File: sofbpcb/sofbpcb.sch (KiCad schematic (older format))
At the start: 18 parts, among them J1 MAX98357A_hdr, J2 MPU6050_hdr, J3 Conn_01x02_Male, J4 LEDStalk_hdr, J5 VibrationMotor_hdr, U1 Teensy4.1, U2 ULN2003

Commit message: Tweak to schematic pwr in
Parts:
- removed J3: Conn_01x02_Male, symbol Connector:Conn_01x02_Male
- added J3: 5v Power In, symbol Connector_Generic:Conn_01x02
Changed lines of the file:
@@
 Date "2021-07-14"
 Rev "1"
-Comp ""
+Comp "Phil McCarthy"
 Comment1 ""
 Comment2 ""
@@
 	5100 6300 5100 6450
 Connection ~ 5100 6450
-$Comp
-L Connector:Conn_01x02_Male J3
-U 1 1 60F0FC2F
-P 5500 6650
-F 0 "J3" V 5654 6462 50  0000 R CNN
-F 1 "Conn_01x02_Male" V 5563 6462 50  0000 R CNN
-F 2 "" H 5500 6650 50  0001 C CNN
-F 3 "~" H 5500 6650 50  0001 C CNN
-	1    5500 6650
-	0    -1   -1   0
-$EndComp
 Wire Wire Line
 	6600 6450 5600 6450
@@
 	1    0    0    -1
 $EndComp
-Connection ~ 5500 6450
 Wire Wire Line
 	4900 3400 5550 3400
 Connection ~ 4900 3400
+$Comp
+L Connector_Generic:Conn_01x02 J3
+U 1 1 60F0E3AF
+P 5600 6650
+F 0 "J3" V 5472 6730 50  0000 L CNN
+F 1 "5v Power In" V 5563 6730 50  0000 L CNN
+F 2 "" H 5600 6650 50  0001 C CNN
+F 3 "~" H 5600 6650 50  0001 C CNN
+	1    5600 6650
+	0    1    1    0
+$EndComp
+Connection ~ 5500 6450
 $EndSCHEMATC

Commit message: Combined led stalk resistors into one
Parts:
- removed R6, R7: 68, symbol Device:R_Small
- R1: value 68 -> 22
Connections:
- net labels added: Cathodes, Led1_Anode, Led2_Anode, Led3_Anode
- net labels removed: ANODES, Led1_Cthd, Led2_Cthd, Led3_Cthd
- wire segments 88 -> 86
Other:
- moved on the sheet: R1
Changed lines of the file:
@@
 L Device:R_Small R1
 U 1 1 60EECD11
-P 7150 2400
-F 0 "R1" H 7209 2446 50  0000 L CNN
-F 1 "68" V 7150 2350 50  0000 L CNN
-F 2 "" H 7150 2400 50  0001 C CNN
-F 3 "~" H 7150 2400 50  0001 C CNN
-	1    7150 2400
-	1    0    0    -1
-$EndComp
-$Comp
-L Device:R_Small R6
-U 1 1 60EECF23
-P 7350 2400
-F 0 "R6" H 7409 2446 50  0000 L CNN
-F 1 "68" V 7350 2350 50  0000 L CNN
-F 2 "" H 7350 2400 50  0001 C CNN
-F 3 "~" H 7350 2400 50  0001 C CNN
-	1    7350 2400
-	1    0    0    -1
-$EndComp
-$Comp
-L Device:R_Small R7
-U 1 1 60EED1C5
-P 7550 2400
-F 0 "R7" H 7609 2446 50  0000 L CNN
-F 1 "68" V 7550 2350 50  0000 L CNN
-F 2 "" H 7550 2400 50  0001 C CNN
-F 3 "~" H 7550 2400 50  0001 C CNN
-	1    7550 2400
+P 7350 3000
+F 0 "R1" H 7409 3046 50  0000 L CNN
+F 1 "22" V 7350 2950 50  0000 L CNN
+F 2 "" H 7350 3000 50  0001 C CNN
+F 3 "~" H 7350 3000 50  0001 C CNN
+	1    7350 3000
 	1    0    0    -1
 $EndComp
@@
 NoConn ~ 1850 4750
 Wire Wire Line
-	7150 2750 7350 2750
-Wire Wire Line
-	7350 2750 7350 3400
-Wire Wire Line
-	7350 3400 6350 3400
-Connection ~ 7350 2750
-Wire Wire Line
 	7550 2750 7350 2750
 $Comp
@@
 $EndComp
 Wire Wire Line
-	7050 1750 7050 3200
-Wire Wire Line
-	7050 3200 6650 3200
-Wire Wire Line
 	6650 2850 6650 3200
 Connection ~ 6650 3200
@@
 $EndComp
 Wire Wire Line
-	7050 3200 7900 3200
-Wire Wire Line
 	7900 3200 7900 3550
-Connection ~ 7050 3200
 Connection ~ 7900 3550
 Wire Wire Line
@@
 Wire Wire Line
 	6550 3800 6350 3800
-Text Label 7050 2050 1    50   ~ 0
-ANODES
-Wire Wire Line
-	7150 2500 7150 2750
-Wire Wire Line
-	7150 1750 7150 2300
-Text Label 7150 2100 1    50   ~ 0
-Led1_Cthd
-Wire Wire Line
-	7350 2500 7350 2750
-Wire Wire Line
-	7550 2500 7550 2750
+Text Label 7150 2150 1    50   ~ 0
+Led1_Anode
 Wire Wire Line
 	7250 1750 7250 2200
 Wire Wire Line
 	7250 2200 7350 2200
-Wire Wire Line
-	7350 2200 7350 2300
-Text Label 7250 2100 1    50   ~ 0
-Led2_Cthd
+Text Label 7250 2150 1    50   ~ 0
+Led2_Anode
 Wire Wire Line
 	7350 1750 7350 2150
 Wire Wire Line
 	7350 2150 7550 2150
-Wire Wire Line
-	7550 2150 7550 2300
-Text Label 7350 2100 1    50   ~ 0
-Led3_Cthd
+Text Label 7350 2150 1    50   ~ 0
+Led3_Anode
 Text Label 7900 4650 0    50   ~ 0
 +
@@
 $EndComp
 Connection ~ 5500 6450
+Wire Wire Line
+	6650 3200 7350 3200
+Wire Wire Line
+	7350 3200 7350 3100
+Connection ~ 7350 3200
+Wire Wire Line
+	7350 3200 7900 3200
+Wire Wire Line
+	7350 2900 7350 2750
+Wire Wire Line
+	7350 2750 7150 2750
+Wire Wire Line
+	7150 1750 7150 2750
+Connection ~ 7350 2750
+Wire Wire Line
+	7350 2200 7350 2750
+Wire Wire Line
+	7550 2150 7550 2750
+Wire Wire Line
+	6350 3400 7050 3400
+Wire Wire Line
+	7050 3400 7050 1750
+Text Label 7050 2050 1    50   ~ 0
+Cathodes
 $EndSCHEMATC

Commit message: pcb mid design. nearly there
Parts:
- removed J4: LEDStalk_hdr, symbol Connector_Generic:Conn_01x04
- removed U1: Teensy4.1, symbol teensy:Teensy4.1
- added J4: LEDStalk_hdr, Connector_JST:JST_XH_S2B-XH-A_1x02_P2.50mm_Horizontal, symbol Connector_Generic:Conn_01x02
- added J6: Teensy4.1_left_hdr, Connector_PinHeader_2.54mm:PinHeader_1x24_P2.54mm_Vertical, symbol Connector_Generic:Conn_01x24
- added J7: Teensy4.1_right_hdr, Connector_PinHeader_2.54mm:PinHeader_1x24_P2.54mm_Vertical, symbol Connector_Generic:Conn_01x24
- D1: footprint (none) -> Diode_THT:D_DO-41_SOD81_P2.54mm_Vertical_AnodeUp
- D2, D3, D4: footprint (none) -> LED_THT:LED_D5.0mm
- J1: footprint (none) -> Connector_PinHeader_2.54mm:PinHeader_1x07_P2.54mm_Vertical
- J2: footprint (none) -> Connector_PinHeader_2.54mm:PinHeader_1x08_P2.54mm_Vertical
- J3, J5: footprint (none) -> Connector_JST:JST_XH_S2B-XH-A_1x02_P2.50mm_Horizontal
- R1: value 22 -> 15; footprint (none) -> Resistor_THT:R_Axial_DIN0207_L6.3mm_D2.5mm_P10.16mm_Horizontal
- R2, R3, R4, R5: footprint (none) -> Resistor_THT:R_Axial_DIN0207_L6.3mm_D2.5mm_P10.16mm_Horizontal
- U2: footprint (none) -> Package_DIP:DIP-16_W7.62mm
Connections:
- net labels added: 3v3, DigAud, GemLED1Sig, GemLED2Sig, GemLED3Sig, LEDStalkSig, LRCLK, VibMtrSig
- net labels removed: Cathodes, DIN, GemLed1, GemLed2, GemLed3, LEDstalk, LRC, Led1_Anode, Led2_Anode, Led3_Anode, VCC, VibMtr
- wire segments 86 -> 64
- no-connect marks 63 -> 44
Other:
- moved on the sheet: D1, D2, D3, D4, J3, J5, R1, R2, R3, R4, R5, U2

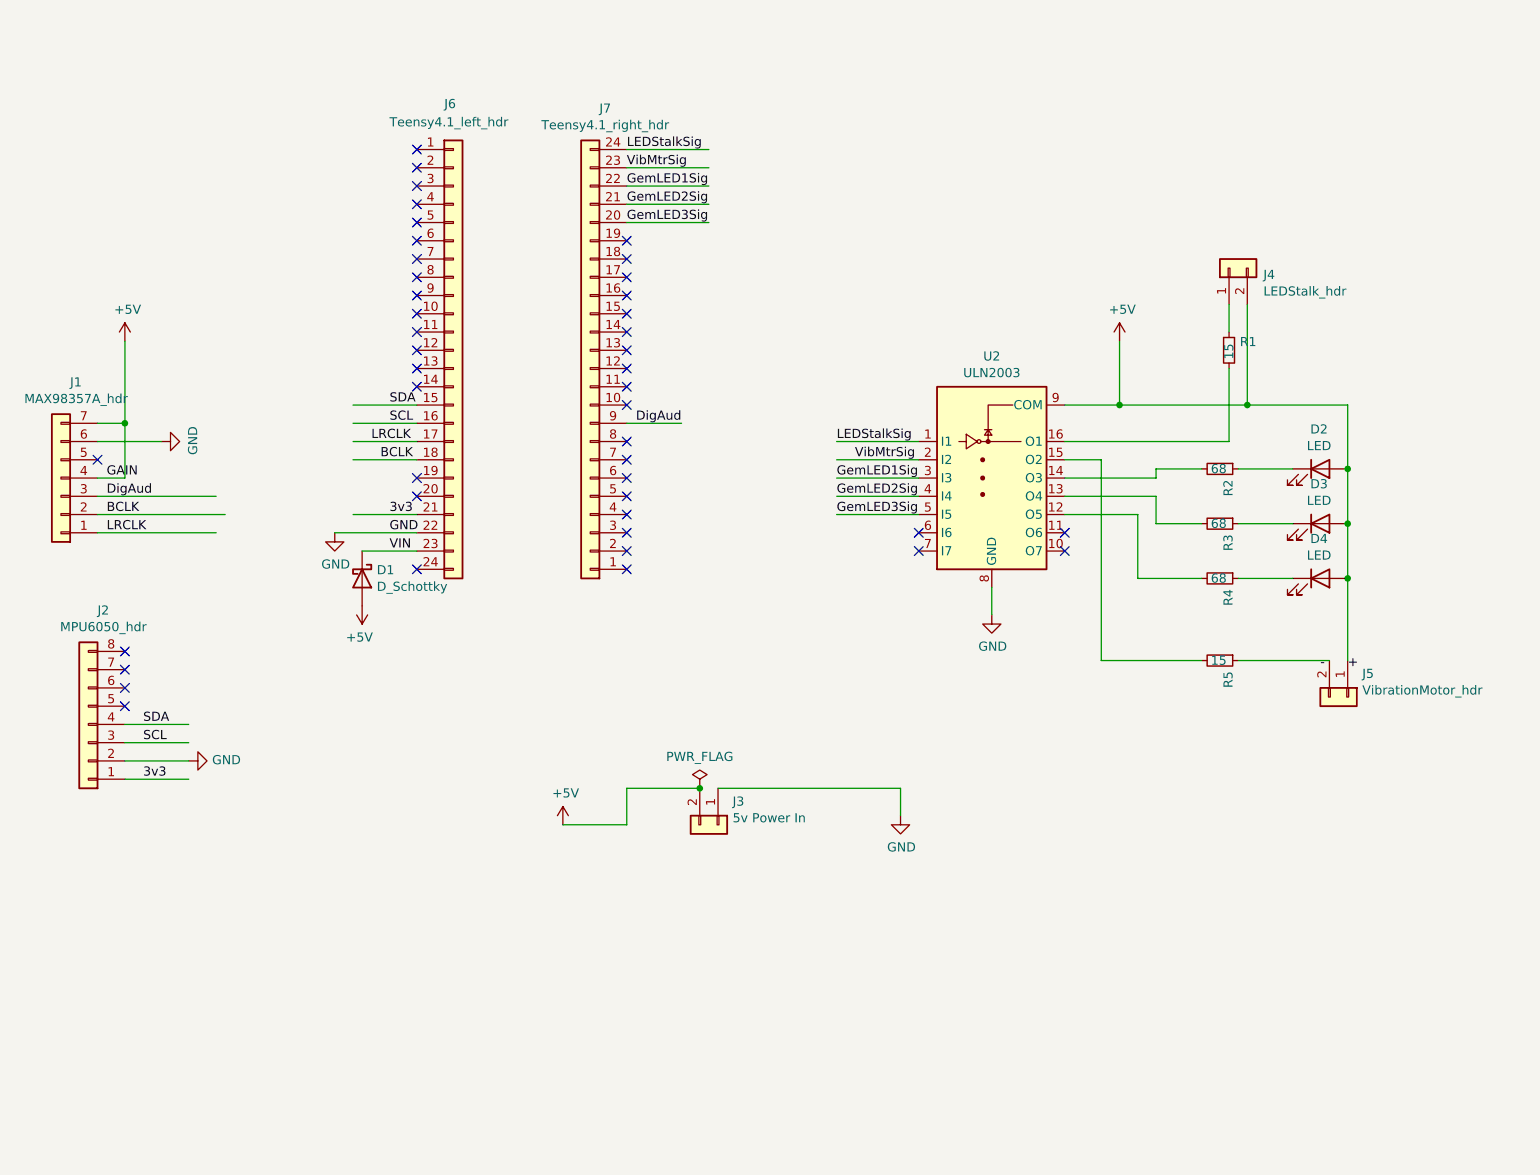
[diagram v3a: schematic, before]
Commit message: PCB design complete, just needs silk screen tidied up
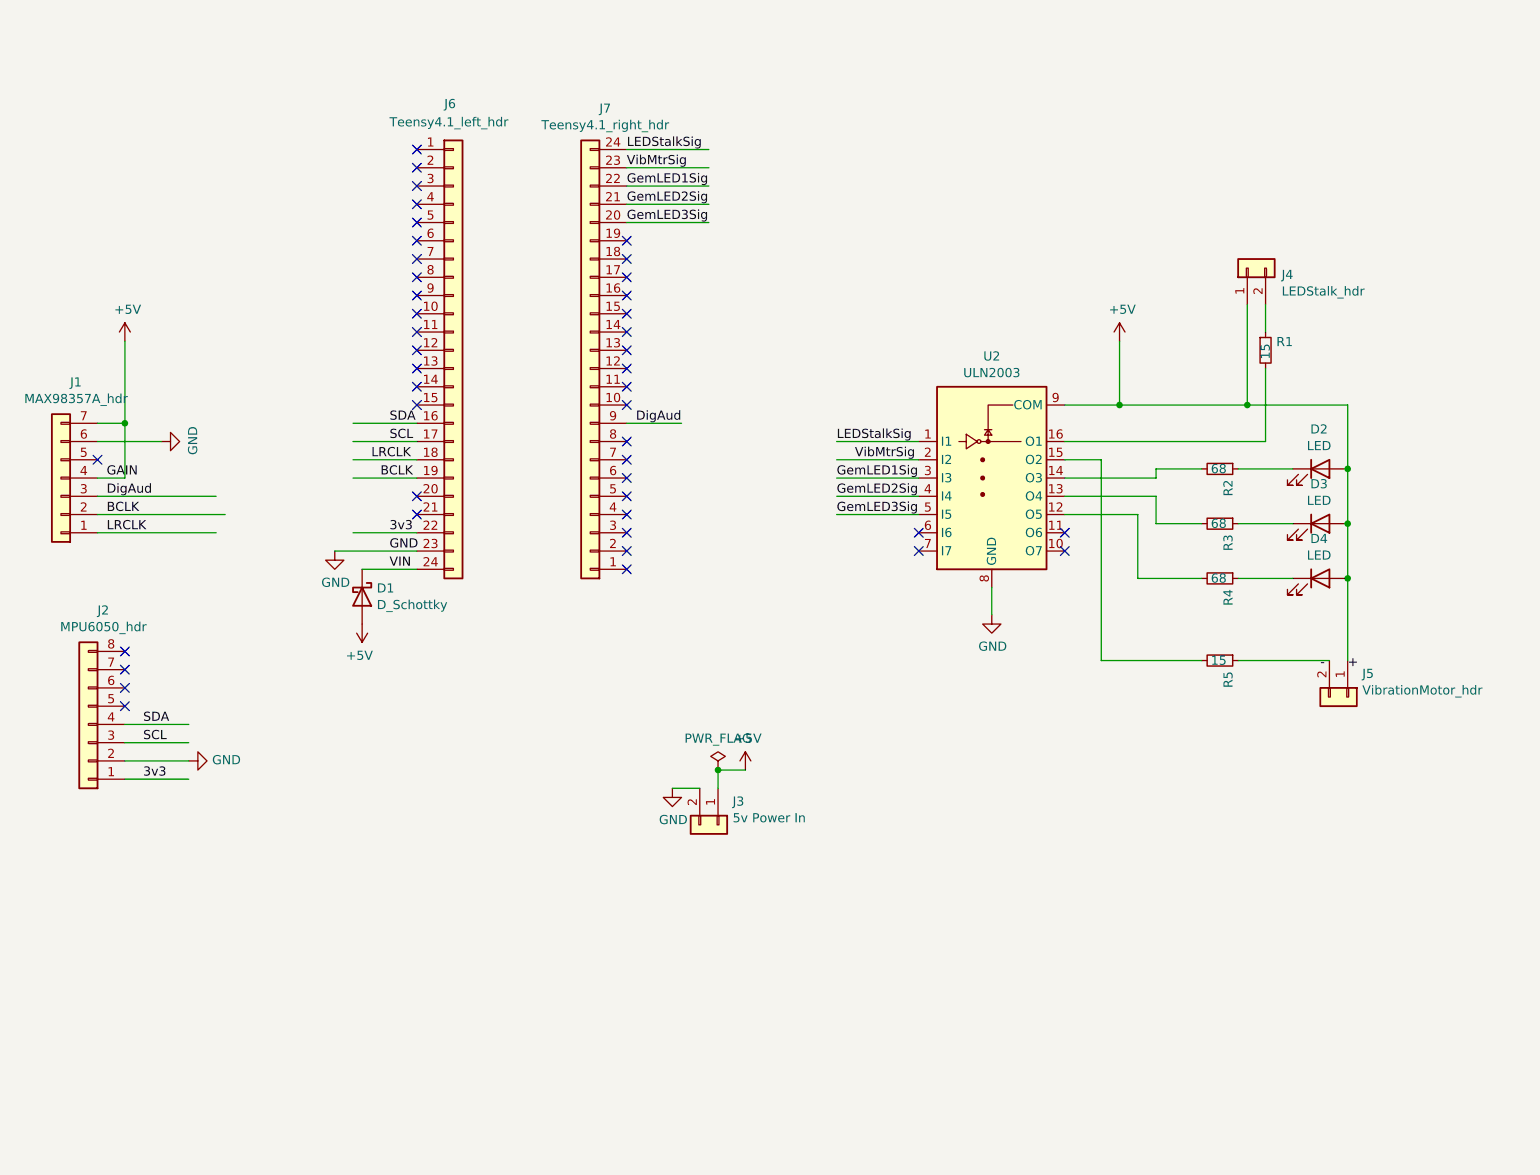
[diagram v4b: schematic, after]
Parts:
- D1: footprint Diode_THT:D_DO-41_SOD81_P2.54mm_Vertical_AnodeUp -> Diode_THT:D_DO-41_SOD81_P10.16mm_Horizontal
- D2, D3, D4: footprint LED_THT:LED_D5.0mm -> LED_THT:LED_D3.0mm
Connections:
- wire segments 64 -> 62
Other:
- moved on the sheet: D1, J4, R1
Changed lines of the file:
@@
 L Device:R_Small R1
 U 1 1 60EECD11
-P 7900 2800
-F 0 "R1" H 7959 2846 50  0000 L CNN
-F 1 "15" V 7900 2750 50  0000 L CNN
-F 2 "Resistor_THT:R_Axial_DIN0207_L6.3mm_D2.5mm_P10.16mm_Horizontal" H 7900 2800 50  0001 C CNN
-F 3 "~" H 7900 2800 50  0001 C CNN
-	1    7900 2800
+P 8100 2800
+F 0 "R1" H 8159 2846 50  0000 L CNN
+F 1 "15" V 8100 2750 50  0000 L CNN
+F 2 "Resistor_THT:R_Axial_DIN0207_L6.3mm_D2.5mm_P10.16mm_Horizontal" H 8100 2800 50  0001 C CNN
+F 3 "~" H 8100 2800 50  0001 C CNN
+	1    8100 2800
 	1    0    0    -1
 $EndComp
@@
 $EndComp
 $Comp
-L power:+5V #PWR04
-U 1 1 60F0E30E
-P 4250 5400
-F 0 "#PWR04" H 4250 5250 50  0001 C CNN
-F 1 "+5V" H 4265 5573 50  0000 C CNN
-F 2 "" H 4250 5400 50  0001 C CNN
-F 3 "" H 4250 5400 50  0001 C CNN
-	1    4250 5400
-	1    0    0    -1
-$EndComp
-Wire Wire Line
-	4250 5400 4600 5400
-Wire Wire Line
-	4600 5400 4600 5200
-$Comp
-L power:GND #PWR06
-U 1 1 60F1268D
-P 6100 5350
-F 0 "#PWR06" H 6100 5100 50  0001 C CNN
-F 1 "GND" H 6105 5177 50  0000 C CNN
-F 2 "" H 6100 5350 50  0001 C CNN
-F 3 "" H 6100 5350 50  0001 C CNN
-	1    6100 5350
-	1    0    0    -1
-$EndComp
-Wire Wire Line
-	6100 5350 6100 5200
-Wire Wire Line
-	4600 5200 5000 5200
-$Comp
 L Device:D_Schottky D1
 U 1 1 60F14A12
-P 3150 4050
-F 0 "D1" V 3104 4130 50  0000 L CNN
-F 1 "D_Schottky" V 3195 4130 50  0000 L CNN
-F 2 "Diode_THT:D_DO-41_SOD81_P2.54mm_Vertical_AnodeUp" H 3150 4050 50  0001 C CNN
-F 3 "~" H 3150 4050 50  0001 C CNN
-	1    3150 4050
-	0    1    1    0
-$EndComp
-Wire Wire Line
-	6100 5200 5100 5200
+P 3150 4150
+F 0 "D1" V 3104 4230 50  0000 L CNN
+F 1 "D_Schottky" V 3195 4230 50  0000 L CNN
+F 2 "Diode_THT:D_DO-41_SOD81_P10.16mm_Horizontal" H 3150 4150 50  0001 C CNN
+F 3 "~" H 3150 4150 50  0001 C CNN
+	1    3150 4150
+	0    1    1    0
+$EndComp
 Text Label 1950 5150 0    50   ~ 0
 3v3
@@
 F 0 "D2" H 8393 3667 50  0000 C CNN
 F 1 "LED" H 8393 3576 50  0000 C CNN
-F 2 "LED_THT:LED_D5.0mm" H 8400 3450 50  0001 C CNN
+F 2 "LED_THT:LED_D3.0mm" H 8400 3450 50  0001 C CNN
 F 3 "~" H 8400 3450 50  0001 C CNN
 	1    8400 3450
@@
 F 0 "D3" H 8393 3967 50  0000 C CNN
 F 1 "LED" H 8393 3876 50  0000 C CNN
-F 2 "LED_THT:LED_D5.0mm" H 8400 3750 50  0001 C CNN
+F 2 "LED_THT:LED_D3.0mm" H 8400 3750 50  0001 C CNN
 F 3 "~" H 8400 3750 50  0001 C CNN
 	1    8400 3750
@@
 F 0 "D4" H 8393 4267 50  0000 C CNN
 F 1 "LED" H 8393 4176 50  0000 C CNN
-F 2 "LED_THT:LED_D5.0mm" H 8400 4050 50  0001 C CNN
+F 2 "LED_THT:LED_D3.0mm" H 8400 4050 50  0001 C CNN
 F 3 "~" H 8400 4050 50  0001 C CNN
 	1    8400 4050
@@
 L power:PWR_FLAG #FLG0101
 U 1 1 60FD14CB
-P 5000 5200
-F 0 "#FLG0101" H 5000 5275 50  0001 C CNN
-F 1 "PWR_FLAG" H 5000 5373 50  0000 C CNN
-F 2 "" H 5000 5200 50  0001 C CNN
-F 3 "~" H 5000 5200 50  0001 C CNN
-	1    5000 5200
+P 5100 5100
+F 0 "#FLG0101" H 5100 5175 50  0001 C CNN
+F 1 "PWR_FLAG" H 5100 5273 50  0000 C CNN
+F 2 "" H 5100 5100 50  0001 C CNN
+F 3 "~" H 5100 5100 50  0001 C CNN
+	1    5100 5100
 	1    0    0    -1
 $EndComp
@@
 	1    5100 5400
 	0    1    1    0
-$EndComp
-Connection ~ 5000 5200
-$Comp
-L Connector_Generic:Conn_01x24 J6
-U 1 1 60F38009
-P 3650 2800
-F 0 "J6" H 3600 4150 50  0000 L CNN
-F 1 "Teensy4.1_left_hdr" H 3300 4050 50  0000 L CNN
-F 2 "Connector_PinHeader_2.54mm:PinHeader_1x24_P2.54mm_Vertical" H 3650 2800 50  0001 C CNN
-F 3 "~" H 3650 2800 50  0001 C CNN
-	1    3650 2800
-	1    0    0    -1
 $EndComp
 $Comp
@@
 $EndComp
 Wire Wire Line
-	3450 3900 3150 3900
+	3450 4000 3150 4000
 $Comp
 L power:+5V #PWR09
 U 1 1 60F489AD
-P 3150 4200
-F 0 "#PWR09" H 3150 4050 50  0001 C CNN
-F 1 "+5V" H 3165 4373 50  0000 C CNN
-F 2 "" H 3150 4200 50  0001 C CNN
-F 3 "" H 3150 4200 50  0001 C CNN
-	1    3150 4200
+P 3150 4300
+F 0 "#PWR09" H 3150 4150 50  0001 C CNN
+F 1 "+5V" H 3165 4473 50  0000 C CNN
+F 2 "" H 3150 4300 50  0001 C CNN
+F 3 "" H 3150 4300 50  0001 C CNN
+	1    3150 4300
 	-1   0    0    1
 $EndComp
-Text Label 3300 3900 0    50   ~ 0
+Text Label 3300 4000 0    50   ~ 0
 VIN
 $Comp
 L power:GND #PWR08
 U 1 1 60F49B47
-P 3000 3800
-F 0 "#PWR08" H 3000 3550 50  0001 C CNN
-F 1 "GND" H 3005 3627 50  0000 C CNN
-F 2 "" H 3000 3800 50  0001 C CNN
-F 3 "" H 3000 3800 50  0001 C CNN
-	1    3000 3800
-	1    0    0    -1
-$EndComp
-Wire Wire Line
-	3000 3800 3450 3800
+P 3000 3900
+F 0 "#PWR08" H 3000 3650 50  0001 C CNN
+F 1 "GND" H 3005 3727 50  0000 C CNN
+F 2 "" H 3000 3900 50  0001 C CNN
+F 3 "" H 3000 3900 50  0001 C CNN
+	1    3000 3900
+	1    0    0    -1
+$EndComp
+Text Label 3300 3900 0    50   ~ 0
+GND
 Text Label 3300 3800 0    50   ~ 0
-GND
-Wire Wire Line
-	3450 3700 3100 3700
-Text Label 3300 3700 0    50   ~ 0
 3v3
-Wire Wire Line
-	3450 3400 3100 3400
-Text Label 3250 3400 0    50   ~ 0
+Text Label 3250 3500 0    50   ~ 0
 BCLK
-Wire Wire Line
-	3450 3300 3100 3300
-Text Label 3200 3300 0    50   ~ 0
+Text Label 3200 3400 0    50   ~ 0
 LRCLK
-Wire Wire Line
-	3450 3200 3100 3200
+Text Label 3300 3300 0    50   ~ 0
+SCL
 Text Label 3300 3200 0    50   ~ 0
-SCL
-Wire Wire Line
-	3450 3100 3100 3100
-Text Label 3300 3100 0    50   ~ 0
 SDA
 Wire Wire Line
@@
 NoConn ~ 3450 2900
 NoConn ~ 3450 3000
-NoConn ~ 3450 3500
 NoConn ~ 3450 3600
-NoConn ~ 3450 4000
 NoConn ~ 4600 4000
 NoConn ~ 4600 3900
@@
 L Connector_Generic:Conn_01x02 J4
 U 1 1 60FD7075
-P 7900 2350
-F 0 "J4" V 7864 2162 50  0000 R CNN
-F 1 "LEDStalk_hdr" V 7773 2162 50  0000 R CNN
-F 2 "Connector_JST:JST_XH_S2B-XH-A_1x02_P2.50mm_Horizontal" H 7900 2350 50  0001 C CNN
-F 3 "~" H 7900 2350 50  0001 C CNN
-	1    7900 2350
+P 8000 2350
+F 0 "J4" V 7964 2162 50  0000 R CNN
+F 1 "LEDStalk_hdr" V 7873 2162 50  0000 R CNN
+F 2 "Connector_JST:JST_XH_S2B-XH-A_1x02_P2.50mm_Horizontal" H 8000 2350 50  0001 C CNN
+F 3 "~" H 8000 2350 50  0001 C CNN
+	1    8000 2350
 	0    -1   -1   0
 $EndComp
@@
 	7300 3100 8000 3100
 Wire Wire Line
-	7000 3300 7900 3300
-Wire Wire Line
-	7900 3300 7900 2900
-Wire Wire Line
-	7900 2700 7900 2550
+	8100 3300 8100 2900
+Wire Wire Line
+	8100 2700 8100 2550
 Wire Wire Line
 	8000 2550 8000 3100
@@
 Wire Wire Line
 	5750 3700 6200 3700
+$Comp
+L power:+5V #PWR0101
+U 1 1 60F730A9
+P 5250 5100
+F 0 "#PWR0101" H 5250 4950 50  0001 C CNN
+F 1 "+5V" H 5265 5273 50  0000 C CNN
+F 2 "" H 5250 5100 50  0001 C CNN
+F 3 "" H 5250 5100 50  0001 C CNN
+	1    5250 5100
+	1    0    0    -1
+$EndComp
+$Comp
+L power:GND #PWR0102
+U 1 1 60F73DD9
+P 4850 5200
+F 0 "#PWR0102" H 4850 4950 50  0001 C CNN
+F 1 "GND" H 4855 5027 50  0000 C CNN
+F 2 "" H 4850 5200 50  0001 C CNN
+F 3 "" H 4850 5200 50  0001 C CNN
+	1    4850 5200
+	1    0    0    -1
+$EndComp
+Wire Wire Line
+	5100 5200 5100 5100
+Wire Wire Line
+	5100 5100 5250 5100
+Connection ~ 5100 5100
+Wire Wire Line
+	4850 5200 5000 5200
+Wire Wire Line
+	7000 3300 8100 3300
+NoConn ~ 3450 3700
+Wire Wire Line
+	3000 3900 3450 3900
+Wire Wire Line
+	3450 3800 3100 3800
+Wire Wire Line
+	3450 3500 3100 3500
+Wire Wire Line
+	3450 3400 3100 3400
+Wire Wire Line
+	3450 3300 3100 3300
+Wire Wire Line
+	3450 3200 3100 3200
+$Comp
+L Connector_Generic:Conn_01x24 J6
+U 1 1 60F38009
+P 3650 2800
+F 0 "J6" H 3600 4150 50  0000 L CNN
+F 1 "Teensy4.1_left_hdr" H 3300 4050 50  0000 L CNN
+F 2 "Connector_PinHeader_2.54mm:PinHeader_1x24_P2.54mm_Vertical" H 3650 2800 50  0001 C CNN
+F 3 "~" H 3650 2800 50  0001 C CNN
+	1    3650 2800
+	1    0    0    -1
+$EndComp
+NoConn ~ 3450 3100
 $EndSCHEMATC
